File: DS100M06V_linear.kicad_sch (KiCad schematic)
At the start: 108 parts, among them J1 wire2board, J10 BNC_panel_mount, J11 wire2board, J2 Wire2Board, J3 wire2board, J4 wire2board, J5 Wire2Board, J6 Wire2Board, J7 Wire2Board, J8 red_safety_4mm_connector, J9 black_safety_4mm_connector, Q2 FS8205A, SW1 SW_DPDT_x2, U1 AD8039, U2 TP4056, U4 AD8009, U5 DW01A, U6 TEA1-0505, U7 TLV61070ADBVR

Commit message: Back to linear.
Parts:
- removed L2, L3: 4.7u, Inductor_SMD:L_Bourns_SRN6045TA, symbol solar_push_pull_sym_lib:SRN6045HA-4R7Y
- removed U6: TEA1-0505, Converter_DCDC:Converter_DCDC_TRACO_TEA1-xxxx_THT, symbol Converter_DCDC:TEA1-0505
- added C3: 1u, Resistor_SMD:R_0603_1608Metric_Pad0.98x0.95mm_HandSolder, symbol Device:C
- added PS1: IA0509S, Converter_DCDC:Converter_DCDC_XP_POWER-IAxxxxS_THT, symbol all_symbols_used:IA0509S
- added U3: L7905, Package_TO_SOT_THT:TO-220-3_Horizontal_TabDown, symbol all_symbols_used:L7905
- added U6: L7805, Package_TO_SOT_THT:TO-220-3_Horizontal_TabDown, symbol all_symbols_used:L7805
- SW1: footprint Button_Switch_THT:SW_CuK_JS202011CQN_DPDT_Straight -> Button_Switch_THT:SW_CK_JS202011CQN_DPDT_Straight
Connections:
- net +5V: now also U6.3 (OUT)
- net -5V: now also U3.3 (VO)
- net -BAT: now also Q2.6 (S), Q2.7 (S); no longer Q2.6,7 (S)
- net 0: now also C3.2, PS1.5 (0V), U3.1 (GND), U6.2 (GND); no longer C1.2, C16.1, C17.1, C2.2, C28.2, J5.1 (Pin_1), Q2.2,3 (S), R25.1, R26.1, R27.1, U2.3 (GND), U2.9 (GND), U5.6 (GND), U7.2 (GND)
- net at C17.2, C28.1, R28.2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: now also PS1.1 (+Vin)
- net at C29.1: now also PS1.4 (-Vout), U3.2 (VI)
- new net: C3.1, PS1.6 (+Vout), U6.1 (IN)
- new net Earth: C1.2, C16.1, C17.1, C2.2, C28.2, J5.1 (Pin_1), PS1.2 (-Vin), Q2.2 (S), Q2.3 (S), R25.1, R26.1, R27.1, U2.3 (GND), U2.9 (GND), U5.6 (GND), U7.2 (GND)
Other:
- moved on the sheet: C16, C29, C30

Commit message: Ill flip ya for it.
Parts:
- added H5, H6, H7, H8: WireFeedHole, MountingHole:MountingHole_2.2mm_M2_ISO7380, symbol Mechanical:MountingHole
- J9: footprint DS100M06V_linear:black_safety_4mm_connector -> DS100M06V_linear:red_safety_4mm_connector
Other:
- moved on the sheet: H1, H3, J3, J4, J8, J9, R8

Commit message: Veći prekidač.
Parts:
- SW1: footprint Button_Switch_THT:SW_CK_JS202011CQN_DPDT_Straight -> DS100M06V_linear:DPDT_bigger
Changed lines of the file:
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@@
 			)
 		)
-		(property "Footprint" "Button_Switch_THT:SW_CK_JS202011CQN_DPDT_Straight"
+		(property "Footprint" "DS100M06V_linear:DPDT_bigger"
 			(at 279.4 83.82 0)
 			(effects
@@
 			)
 		)
-		(property "Footprint" "Button_Switch_THT:SW_CK_JS202011CQN_DPDT_Straight"
+		(property "Footprint" "DS100M06V_linear:DPDT_bigger"
 			(at 279.4 127 0)
 			(effects

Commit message: Img tst
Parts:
- removed C16, C20: 1n, Resistor_SMD:R_0603_1608Metric_Pad0.98x0.95mm_HandSolder, symbol Device:C
- removed RV3: 100, Potentiometer_THT:Potentiometer_Bourns_3296W_Vertical, symbol Device:R_Potentiometer
- added C19: 1u, Resistor_SMD:R_0603_1608Metric_Pad0.98x0.95mm_HandSolder, symbol Device:C
- added C20, C36, C40: 470u, Capacitor_THT:CP_Radial_D8.0mm_P3.50mm, symbol Device:C_Polarized_US
- added C33, C4: 100n, Resistor_SMD:R_0603_1608Metric_Pad0.98x0.95mm_HandSolder, symbol Device:C
- added C34: 1n, Resistor_SMD:R_0603_1608Metric_Pad0.98x0.95mm_HandSolder, symbol Device:C
- added C41, C42, C43: 10u, Resistor_SMD:R_1206_3216Metric_Pad1.30x1.75mm_HandSolder, symbol Device:C
- added L2: 4.7u, Inductor_THT:L_Radial_D7.5mm_P3.50mm_Fastron_07P, symbol Device:L
- added SW2: SW_DPDT_x2, DS100M06V_linear:DPDT_bigger, symbol Switch:SW_DPDT_x2
- C17, C26: value 1n -> 1u
- C18, C21: value 1u -> 100n
- C35, C37: value 1u -> 1n
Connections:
- net +5V: now also TP3.1, C19.2, C33.2, C34.2, C36.1
- net +BAT: now also SW2.3 (C); no longer L1.1, U7.3 (EN), U7.6 (VI)
- net -5V: now also C20.1; no longer TP3.1
- net 0: now also C19.1, C20.2, C33.1, C34.1, C36.2, C4.1; no longer RV2.1
- net Earth: now also C40.2, C41.1, C42.1, C43.1
- net at R12.1: now also RV2.1
- net at C17.2, C28.1, PS1.1 (+Vin)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: now also C40.1, C41.2, C42.2
- net at R24.1, RV4.2: now also C4.2
- net at L1.2, U7.1 (SW): now also L2.2
- new net: C43.2, L1.1, L2.1, SW2.2 (B), U7.3 (EN), U7.6 (VI)
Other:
- note removed: "add 5V boost"
- moved on the sheet: C18, C2, C21, C22, C25, C26, C27, C35, C37, C38, L1, Q2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

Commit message: Layout skoro gotov.
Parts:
- C27: value 1n -> 1u
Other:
- note removed: "missing protection"
- moved on the sheet: C1, C10, C11, C12, C13, C14, C15, C17, C18, C19, C2, C20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

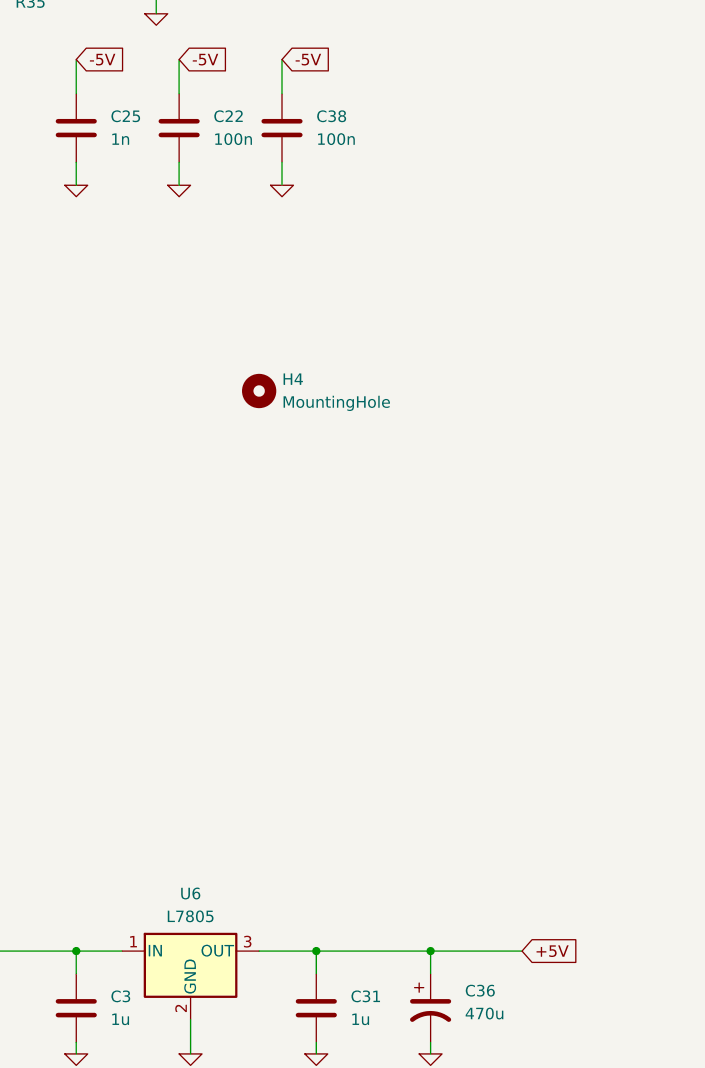
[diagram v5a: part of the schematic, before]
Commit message: Added PCB spacers.
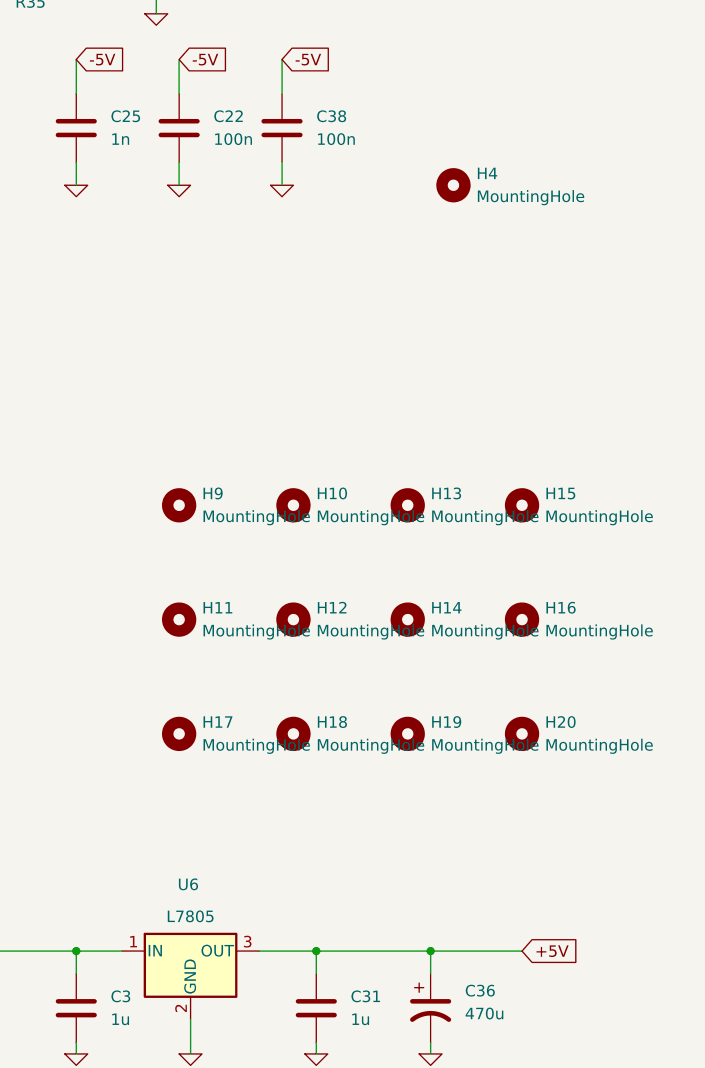
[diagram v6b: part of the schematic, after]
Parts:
- added H10, H11, H12, H13, H14, H15, H16, H17, H18, H19, H20, H9: MountingHole, MountingHole:MountingHole_3.2mm_M3, symbol Mechanical:MountingHole
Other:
- moved on the sheet: H4

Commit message: cap mult sim.
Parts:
- added Q1: BD679, Package_TO_SOT_THT:TO-126-3_Horizontal_TabUp, symbol DS100M06V_linear:BD679
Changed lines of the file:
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@@
+	)
+	(symbol
+		(lib_id "DS100M06V_linear:BD679")
+		(at 248.92 158.75 0)
+		(unit 1)
+		(exclude_from_sim no)
+		(in_bom yes)
+		(on_board yes)
+		(dnp no)
+		(fields_autoplaced yes)
+		(property "Reference" "Q1"
+			(at 254 157.4799 0)
+			(effects
+				(font
+					(size 1.27 1.27)
+				)
+				(justify left)
+			)
+		)
+		(property "Value" "BD679"
+			(at 254 160.0199 0)
+			(effects
+				(font
+					(size 1.27 1.27)
+				)
+				(justify left)
+			)
+		)
+		(property "Footprint" "Package_TO_SOT_THT:TO-126-3_Horizontal_TabUp"
+			(at 254 156.21 0)
+			(effects
+				(font
+					(size 1.27 1.27)
+				)
+				(hide yes)
+			)
+		)
+		(property "Datasheet" "~"
+			(at 248.92 158.75 0)
+			(effects
+				(font
+					(size 1.27 1.27)
+				)
+				(hide yes)
+			)
+		)
+		(property "Description" "NPN Darlington transistor, base/collector/emitter"
+			(at 248.92 158.75 0)
+			(effects
+				(font
+					(size 1.27 1.27)
+				)
+				(hide yes)
+			)
+		)
+		(pin "2"
+		)
+		(pin "3"
+		)
+		(pin "1"
+		)
+		(instances
+			(project ""
+				(path "/e034a6c3-9973-4355-8043-c1e988e27610"
+					(reference "Q1")
+					(unit 1)
+				)
+			)
+		)
 	)
 	(symbol

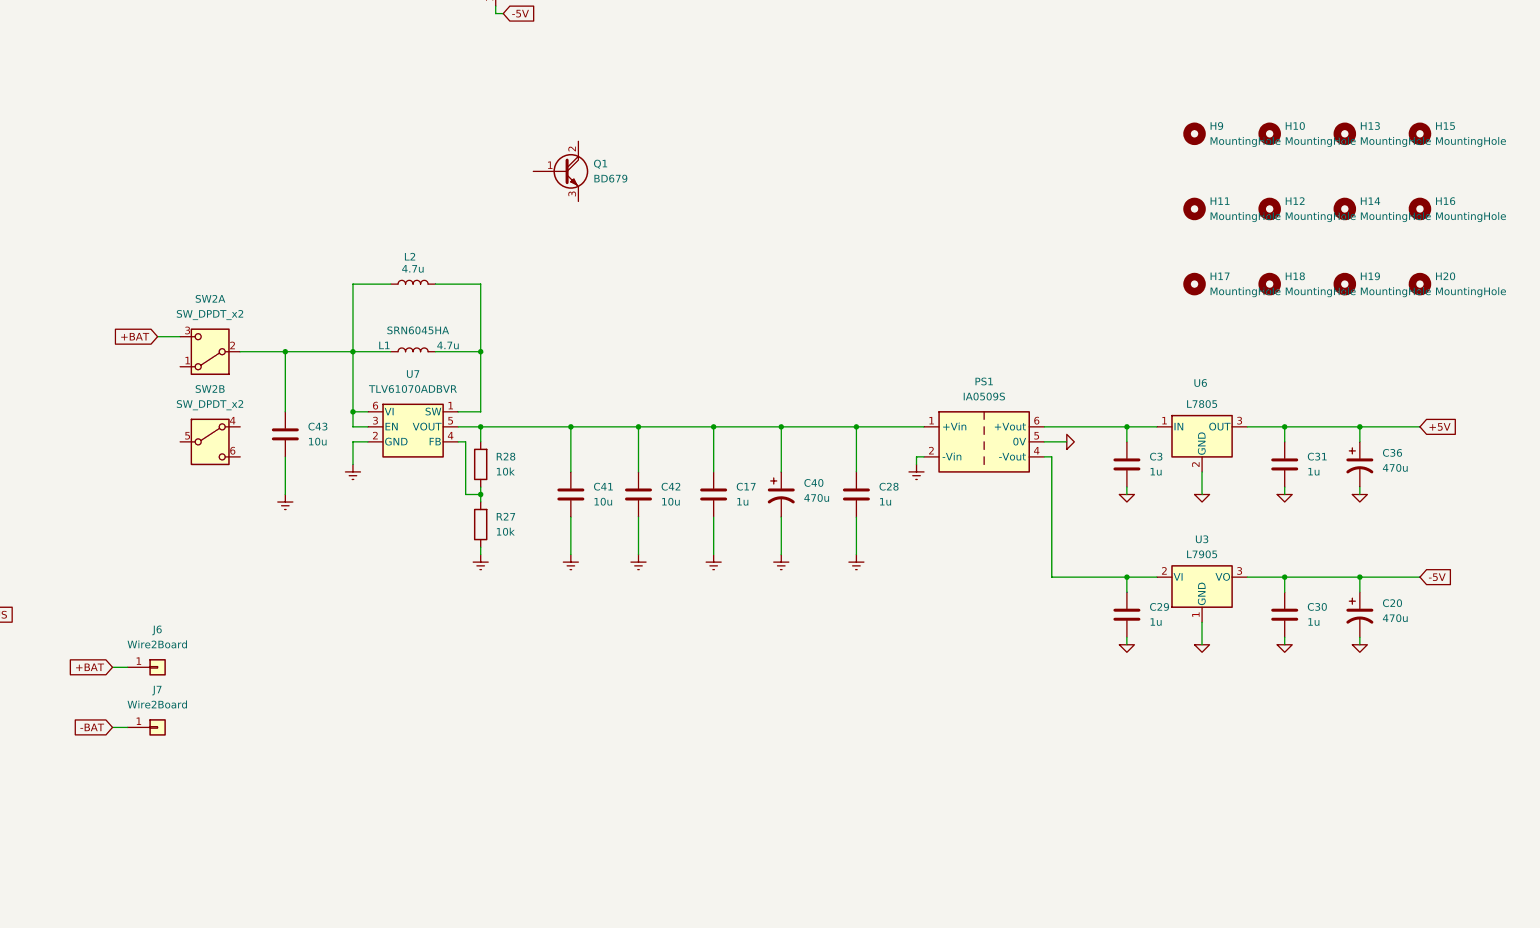
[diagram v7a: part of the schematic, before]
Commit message: Added capacitance multiplier.
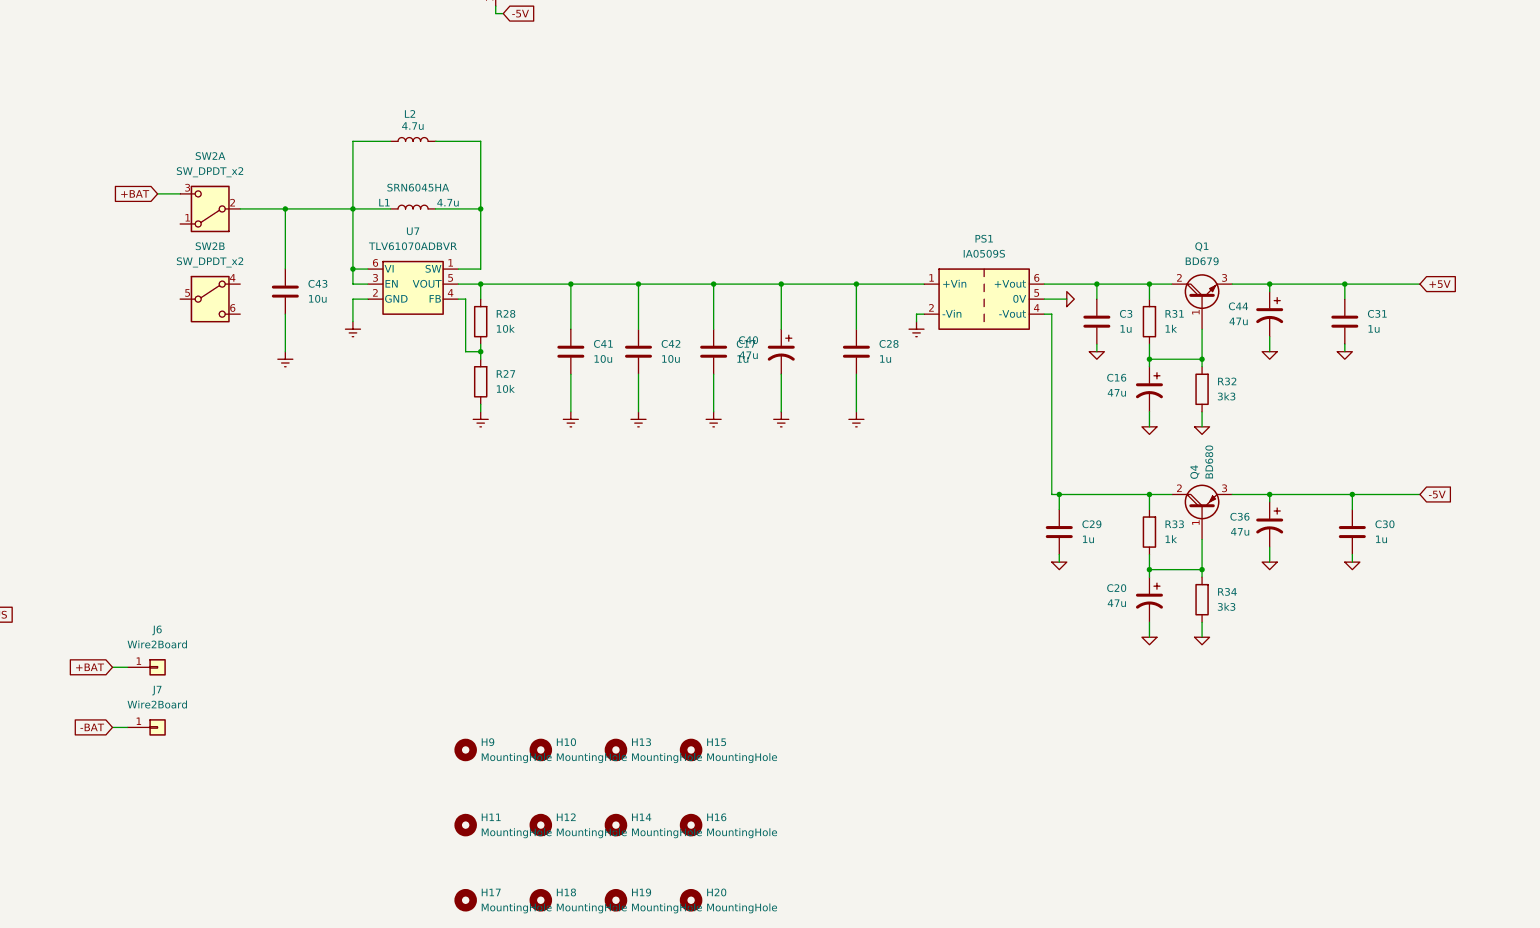
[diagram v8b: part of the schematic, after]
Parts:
- removed U3: L7905, Package_TO_SOT_THT:TO-220-3_Horizontal_TabDown, symbol all_symbols_used:L7905
- removed U6: L7805, Package_TO_SOT_THT:TO-220-3_Horizontal_TabDown, symbol all_symbols_used:L7805
- added C16, C44: 47u, Capacitor_THT:CP_Radial_D5.0mm_P2.00mm, symbol Device:C_Polarized_US
- added Q4: BD680, Package_TO_SOT_THT:TO-126-3_Horizontal_TabUp, symbol DS100M06V_linear:BD680
- added R31, R33: 1k, Resistor_SMD:R_0603_1608Metric_Pad0.98x0.95mm_HandSolder, symbol Device:R
- added R32, R34: 3k3, Resistor_SMD:R_0603_1608Metric_Pad0.98x0.95mm_HandSolder, symbol Device:R
- C20, C36, C40: value 470u -> 47u; footprint Capacitor_THT:CP_Radial_D8.0mm_P3.50mm -> Capacitor_THT:CP_Radial_D5.0mm_P2.00mm
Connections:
- net +5V: now also Q1.3 (E), C44.1; no longer C36.1
- net -5V: now also C36.1, Q4.3 (E); no longer C20.1
- net 0: now also C16.2, C44.2, R32.1, R34.1
- net at C3.1, PS1.6 (+Vout): now also Q1.2 (C), R31.2
- net at Q1.1 (B): now also C16.1, R31.1, R32.2
- net at C29.1, PS1.4 (-Vout): now also Q4.2 (C), R33.2
- new net: C20.1, Q4.1 (B), R33.1, R34.2
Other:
- moved on the sheet: C17, C28, C29, C3, C30, C31, C41, C42, C43, H10, H11, H12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
